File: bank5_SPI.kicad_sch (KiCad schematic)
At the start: 18 parts, among them U1 NX1H35 PBGA625, U5 CY15B108QN-40SXI, U6 CY15B108QN-40SXI, U7 CY15B108QN-40SXI

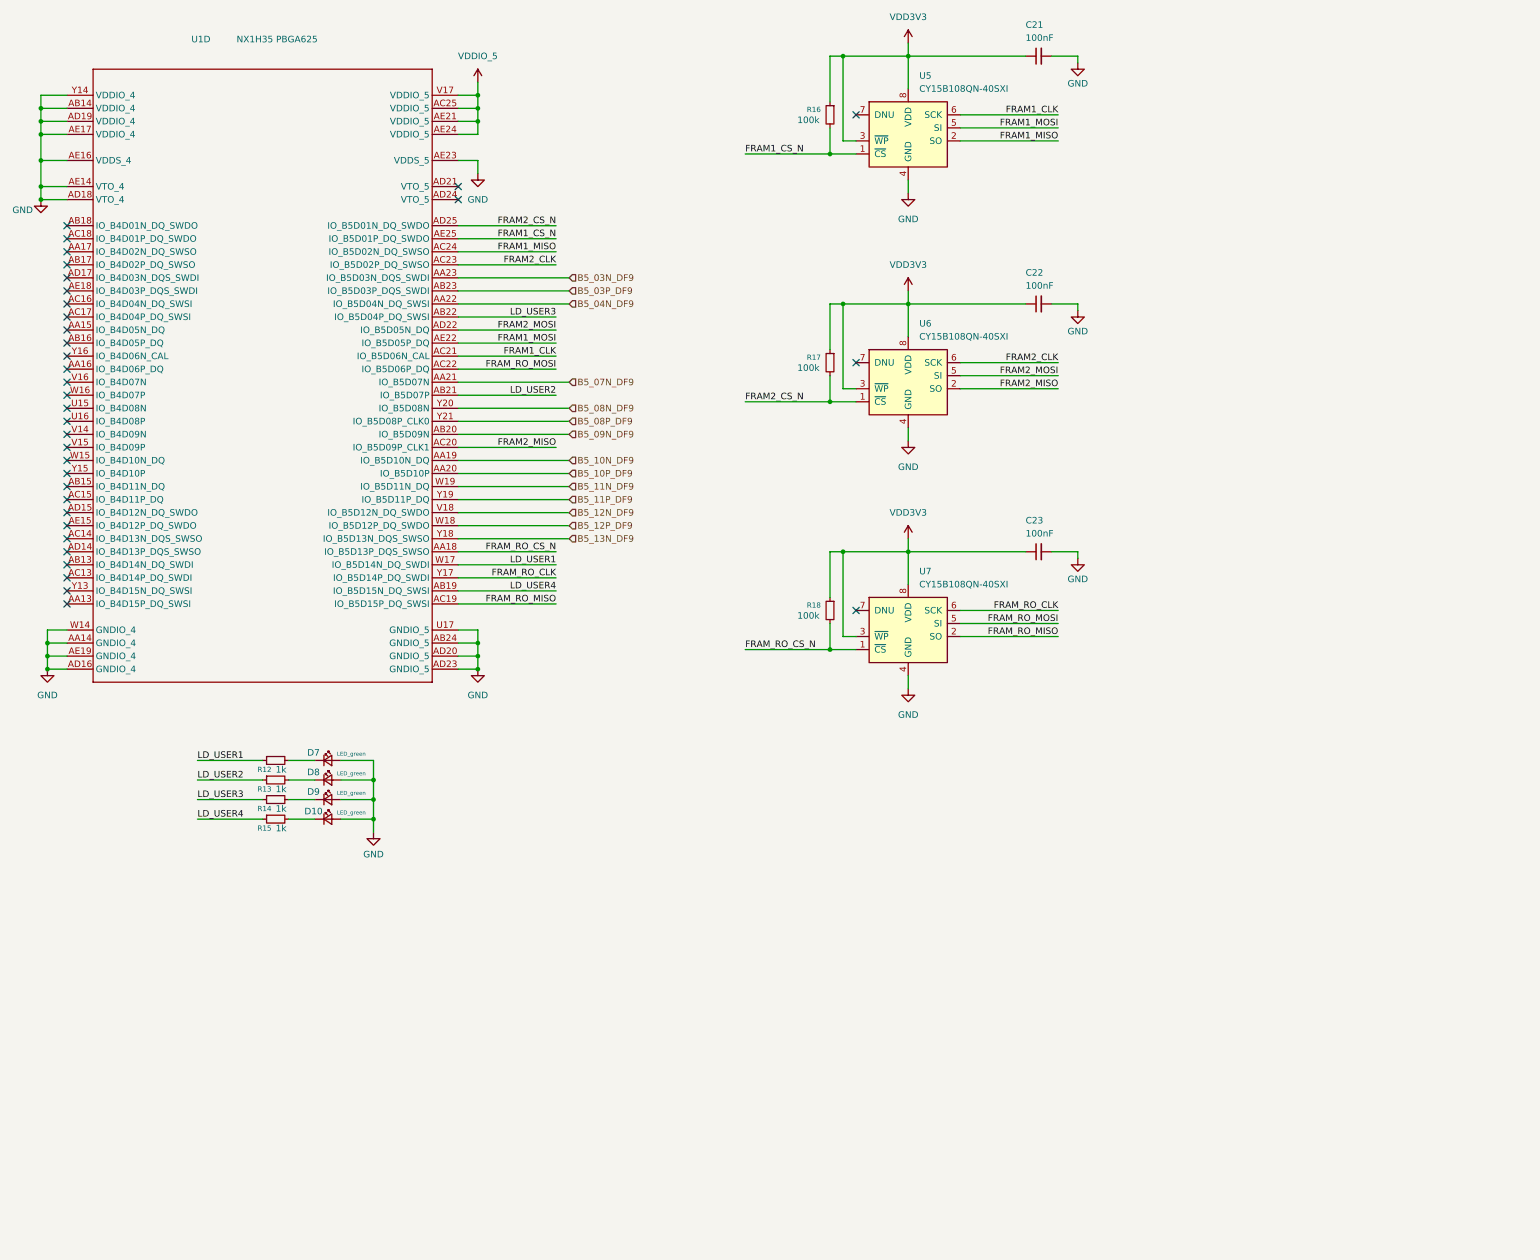
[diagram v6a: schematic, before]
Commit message: pre order adjustments. Board symmetry
adjusted little things brought up by DFM checker of JLCPCB. Board's edges fully symmetrical on y axis. 2mm shift on x axis of the DF9s maintained
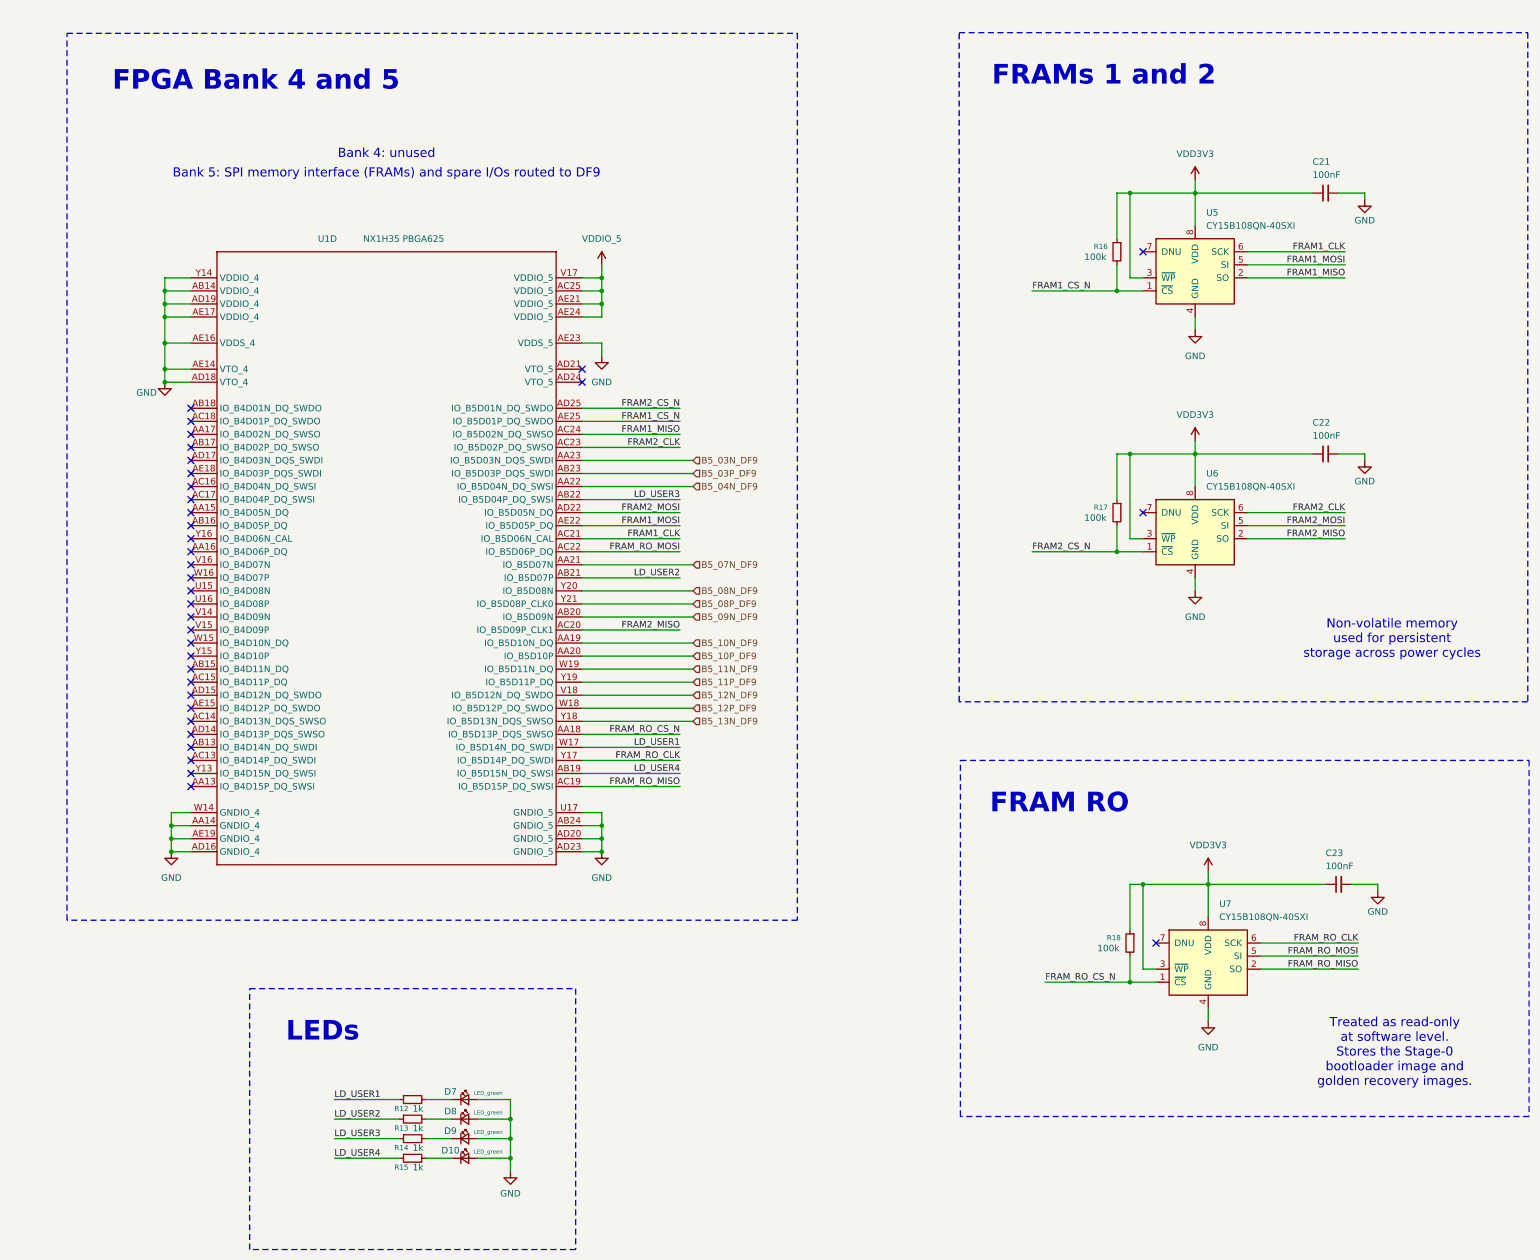
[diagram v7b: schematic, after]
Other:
- note added: "Bank 4: unused"
- note added: "Bank 5: SPI memory interface (FRAMs) and spare I/Os routed to DF9"
- note added: "FPGA Bank 4 and 5"
- note added: "FRAM RO"
- note added: "FRAMs 1 and 2"
- note added: "LEDs"
- note added: "Non-volatile memory used for persistent storage across power cycles"
- note added: "Treated as read-only at software level. Stores the Stage-0 bootloader image and golden recovery images."
- moved on the sheet: C21, C22, C23, D10, D7, D8, D9, R12, R13, R14, R15, R16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
